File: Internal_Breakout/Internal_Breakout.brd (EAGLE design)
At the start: 50 x 35 mm, 21 parts, among them Q1 DMP3099L, U1 LP2985

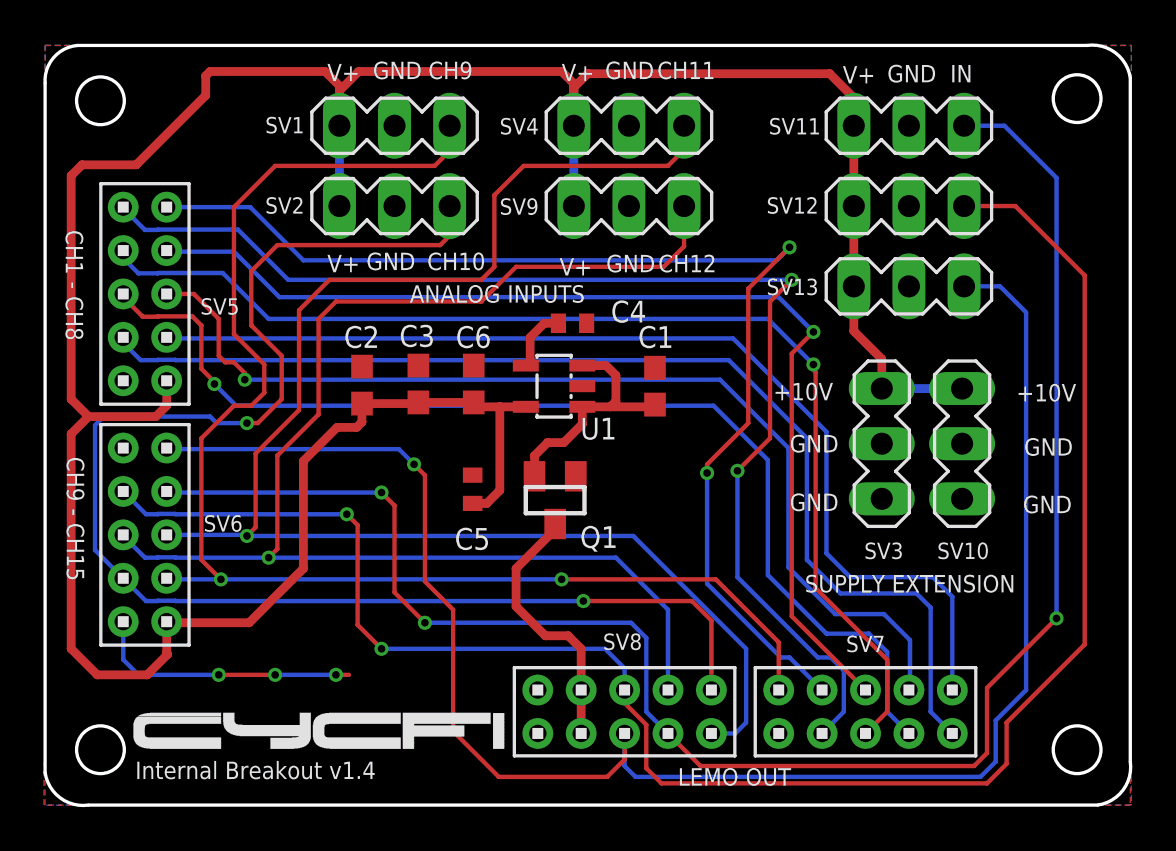
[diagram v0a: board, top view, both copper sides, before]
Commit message: Fixed labels on internal breakout
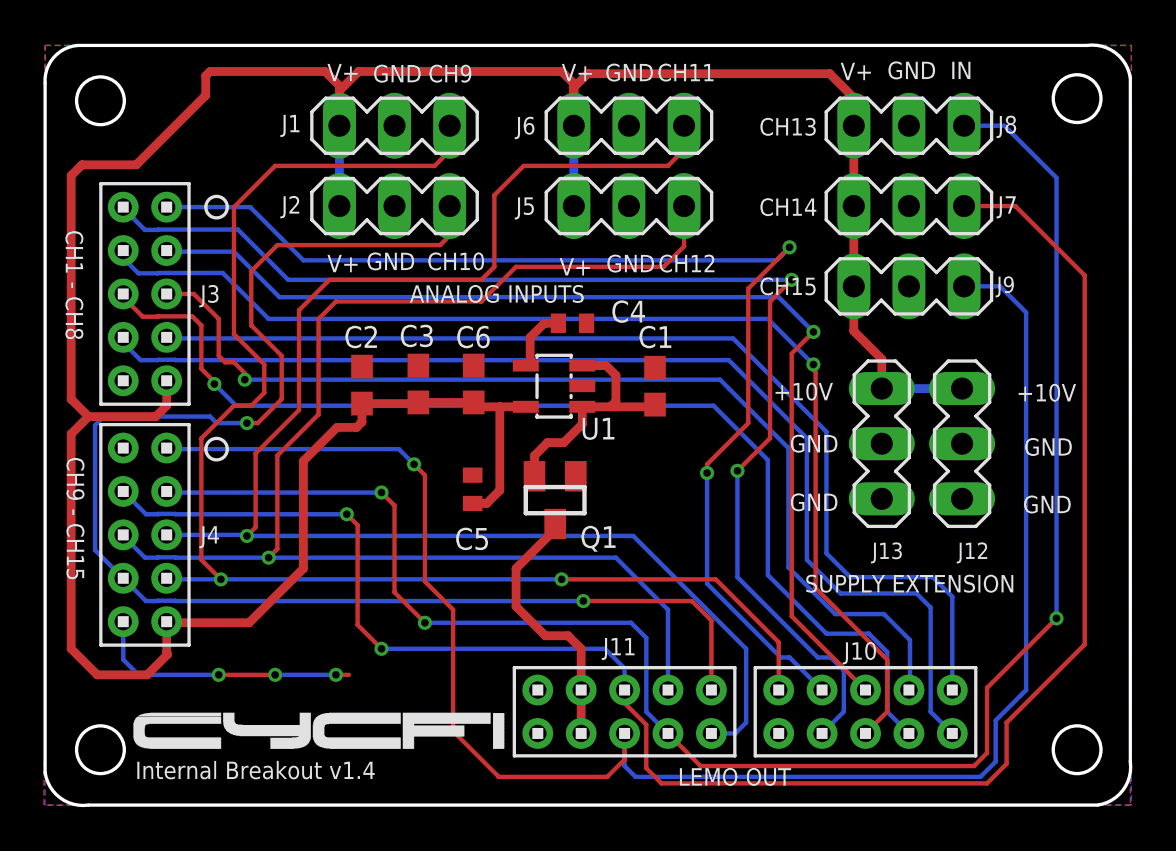
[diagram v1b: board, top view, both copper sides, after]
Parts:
- renumbered SV1 to J1, SV10 to J12, SV11 to J8, SV12 to J7, SV13 to J9, SV2 to J2, SV3 to J13, SV4 to J6, SV5 to J3, SV6 to J4, SV7 to J10, SV8 to J11, SV9 to J5
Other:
- board text added: "CH13"
- board text added: "CH14"
- board text added: "CH15"
- board text added: "J10"
- board text added: "J11"
- board text added: "J3"
- board text added: "J4"
- board text removed: "SV5"
- board text removed: "SV6"
- board text removed: "SV7"
- board text removed: "SV8"

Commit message: fix schematic issue, connector's triangle marking must to pin 1 of the header in the schematic
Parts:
- flipped J10 to the bottom, turned to 0 degrees
- flipped J11 to the bottom, turned to 0 degrees
- flipped J3 to the bottom, turned to 270 degrees
- flipped J4 to the bottom, turned to 270 degrees
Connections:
- net +VDC_IN renamed VCC
- removed net N$2: J4.10
- new net NC: J4.2
- net CH1: now also J10.2, J3.7; no longer J10.1, J3.3
- net CH10: now also J11.2, J4.8; no longer J11.1, J4.4
- net CH11: now also J11.1; no longer J11.2
- net CH12: now also J11.4; no longer J11.3
- net CH13: now also J11.3, J4.3; no longer J11.4, J4.7
- net CH14: now also J11.6, J4.4; no longer J11.5, J4.8
- net CH15: now also J11.5, J4.1; no longer J11.6, J4.9
- net CH2: now also J10.1, J3.8; no longer J10.2, J3.4
- net CH3: now also J10.4; no longer J10.3
- net CH4: now also J10.3; no longer J10.4
- net CH5: now also J10.6, J3.3; no longer J10.5, J3.7
- net CH6: now also J10.5, J3.4; no longer J10.6, J3.8
- net CH7: now also J10.8, J3.1; no longer J10.7, J3.9
- net CH8: now also J10.7, J3.2; no longer J10.8, J3.10
- net CH9: now also J10.10, J4.7; no longer J10.9, J4.3
- net GND: now also J10.9, J3.10, J4.10; no longer J10.10, J3.2, J4.2
- net V+: now also J3.9, J4.9; no longer J3.1, J4.1
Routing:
- net GND: track 12.4 -> 0.00 mm, vias 3 -> 0
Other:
- board text added: "Internal Breakout v2.0"
- board text removed: "Internal Breakout v1.4"
